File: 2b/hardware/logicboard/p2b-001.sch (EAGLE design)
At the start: 72 parts, among them IC1 74LS06N, IC2 4066N, J1 MKR, J10 1-Wire, J2 GPIO, J3 Vcc, J4** RLY2, J5 SPI, J6 LED, J7 DIN5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

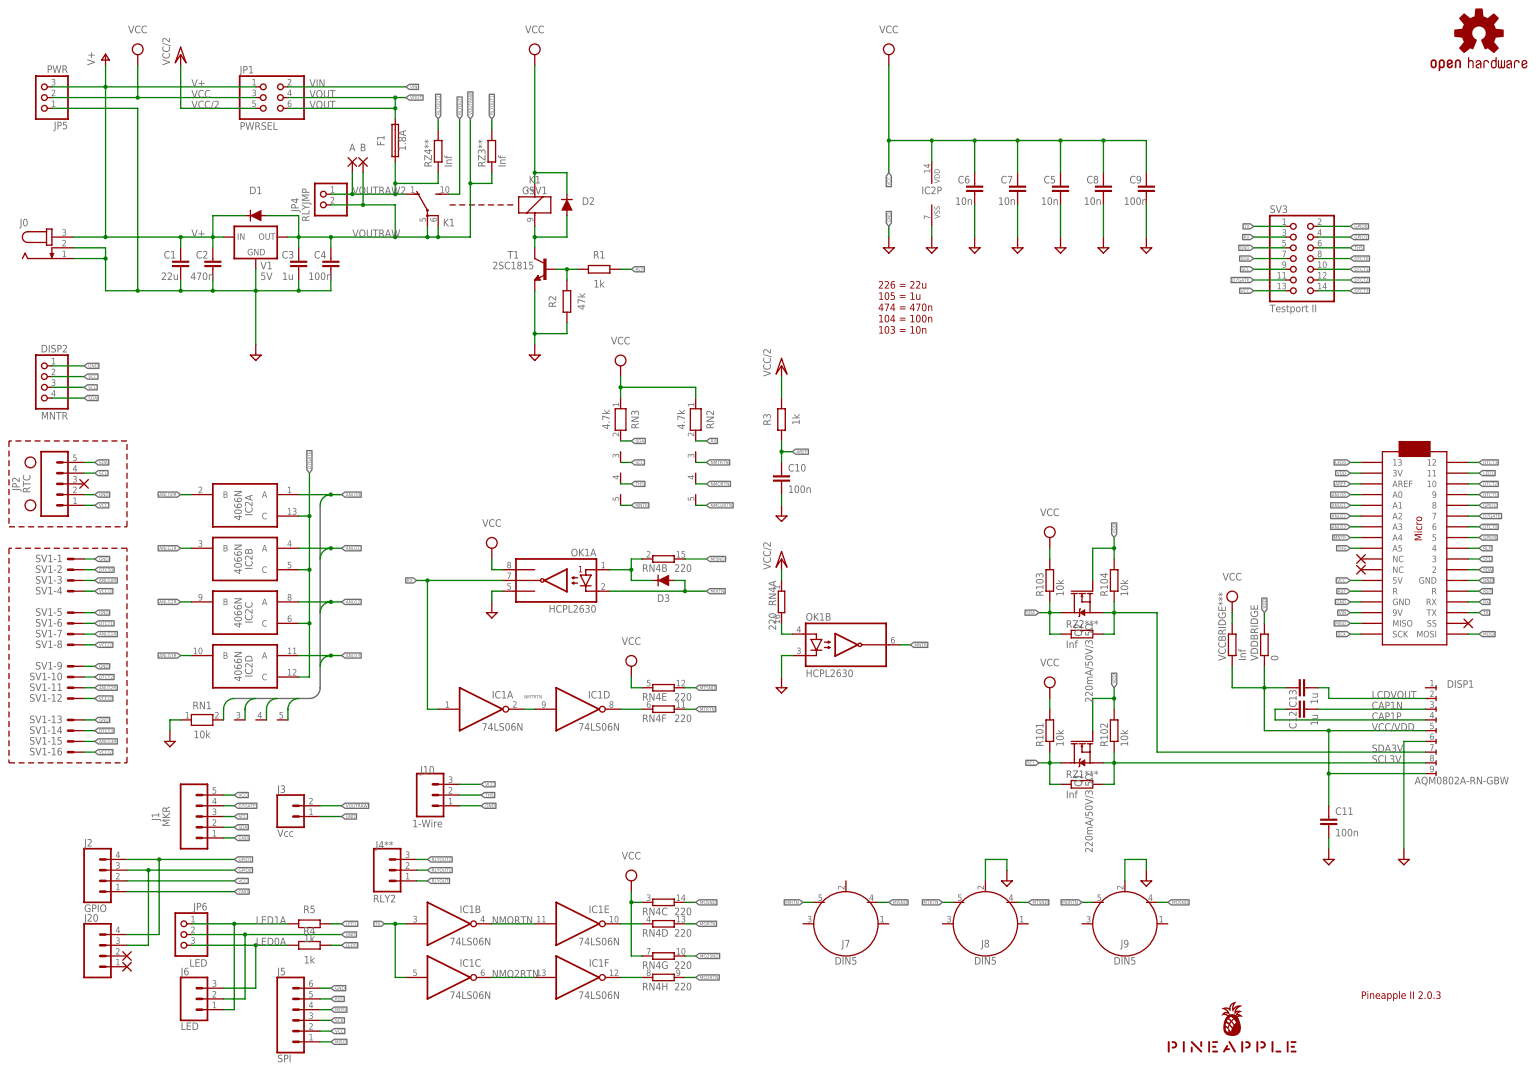
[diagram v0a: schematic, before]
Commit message: Added RST sw to P2b.
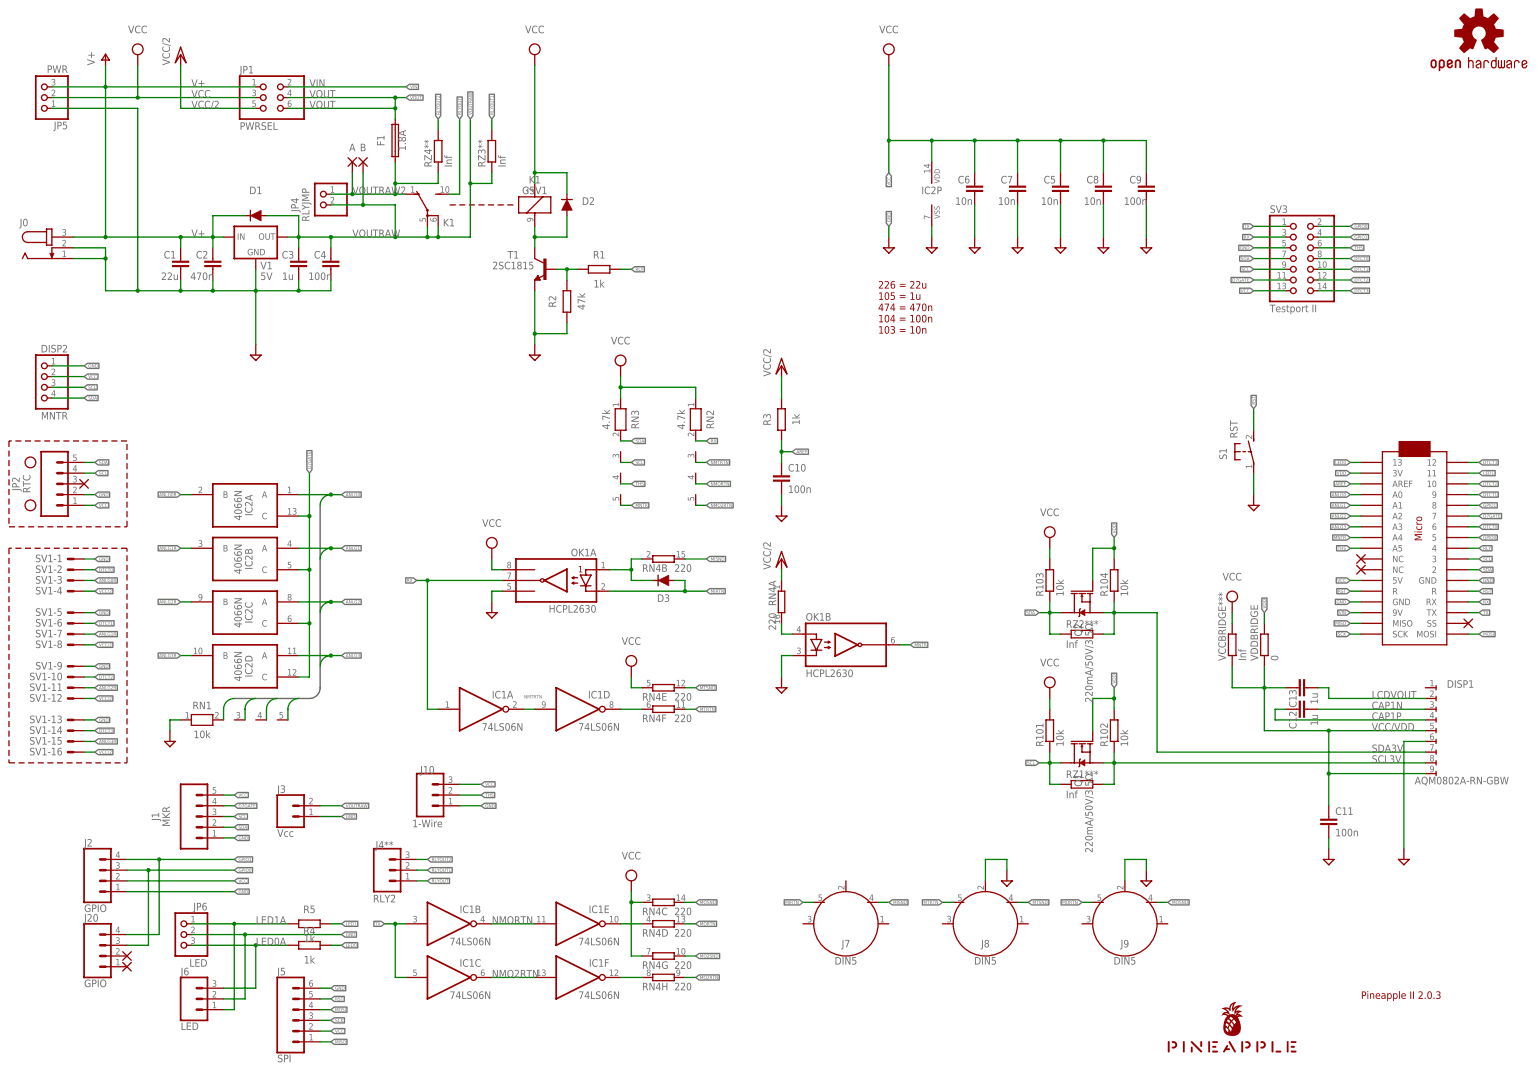
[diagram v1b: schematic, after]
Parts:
- added S1: RST, switch-omron:31-XX
- J20: value (none) -> GPIO
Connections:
- net GND: now also S1.P
- net RST: now also S1.S
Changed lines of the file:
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@@
 <setting verticaltext="up"/>
 </settings>
-<grid distance="0.1" unitdist="inch" unit="inch" style="dots" multiple="1" display="yes" altdistance="0.01" altunitdist="inch" altunit="inch"/>
+<grid distance="0.1" unitdist="inch" unit="inch" style="lines" multiple="1" display="no" altdistance="0.01" altunitdist="inch" altunit="inch"/>
 <layers>
 <layer number="1" name="Top" color="4" fill="1" visible="no" active="no"/>
@@
 <part name="J5" library="SparkFun-Connectors" library_urn="urn:adsk.eagle:library:513" deviceset="CONN_06" device="1.27MM" package3d_urn="urn:adsk.eagle:package:38131/1" value="SPI"/>
 <part name="J10" library="SparkFun-Connectors" library_urn="urn:adsk.eagle:library:513" deviceset="CONN_03" device="JST-PTH-VERT" package3d_urn="urn:adsk.eagle:package:38080/1" value="1-Wire"/>
-<part name="J20" library="SparkFun-Connectors" library_urn="urn:adsk.eagle:library:513" deviceset="CONN_04" device="1.27MM" package3d_urn="urn:adsk.eagle:package:38086/1"/>
+<part name="J20" library="SparkFun-Connectors" library_urn="urn:adsk.eagle:library:513" deviceset="CONN_04" device="1.27MM" package3d_urn="urn:adsk.eagle:package:38086/1" value="GPIO"/>
 <part name="X1" library="wirepad" library_urn="urn:adsk.eagle:library:412" deviceset="PAD-N" device=""/>
 <part name="X2" library="wirepad" library_urn="urn:adsk.eagle:library:412" deviceset="PAD-N" device=""/>
+<part name="S1" library="switch-omron" library_urn="urn:adsk.eagle:library:377" deviceset="31-XX" device="" package3d_urn="urn:adsk.eagle:package:27487/1" value="RST"/>
+<part name="SUPPLY18" library="supply2" deviceset="GND" device=""/>
 </parts>
 <sheets>
@@
 <instance part="X1" gate="G$1" x="50.8" y="30.48" smashed="yes"/>
 <instance part="X2" gate="G$1" x="50.8" y="27.94" smashed="yes"/>
+<instance part="S1" gate="1" x="317.5" y="149.86" smashed="yes">
+<attribute name="NAME" x="311.15" y="147.955" size="1.778" layer="95" rot="R90"/>
+<attribute name="VALUE" x="313.69" y="153.035" size="1.778" layer="96" rot="R90"/>
+</instance>
+<instance part="SUPPLY18" gate="GND" x="317.5" y="137.16" smashed="yes"/>
 </instances>
 <busses>
@@
 <label x="134.62" y="66.04" size="0.8128" layer="95" xref="yes"/>
 </segment>
+<segment>
+<pinref part="S1" gate="1" pin="P"/>
+<wire x1="317.5" y1="144.78" x2="317.5" y2="139.7" width="0.1524" layer="91"/>
+<pinref part="SUPPLY18" gate="GND" pin="GND"/>
+</segment>
 </net>
 <net name="VCC" class="2">
@@
 <pinref part="J5" gate="G$1" pin="5"/>
 </segment>
+<segment>
+<pinref part="S1" gate="1" pin="S"/>
+<wire x1="317.5" y1="154.94" x2="317.5" y2="160.02" width="0.1524" layer="91"/>
+<label x="317.5" y="160.02" size="0.8128" layer="95" rot="R90" xref="yes"/>
+</segment>
 </net>

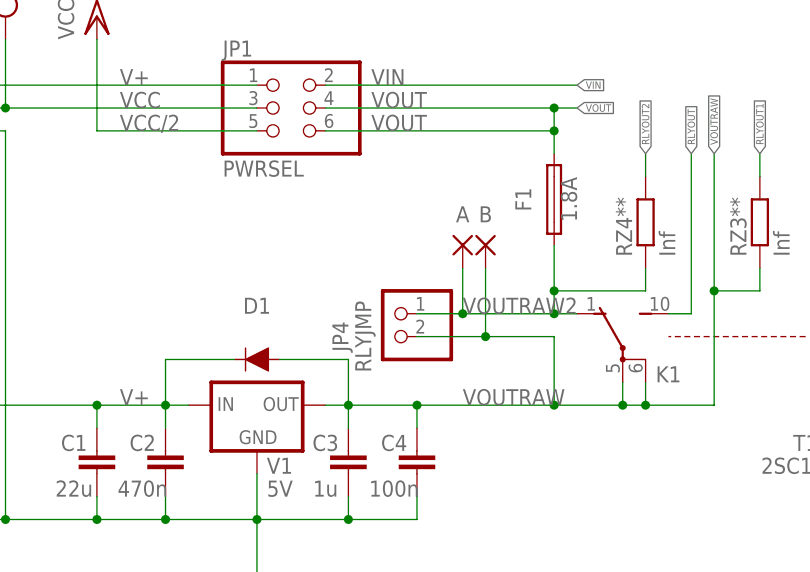
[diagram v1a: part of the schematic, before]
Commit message: Changed pads to Inf-ohm chip resistor.
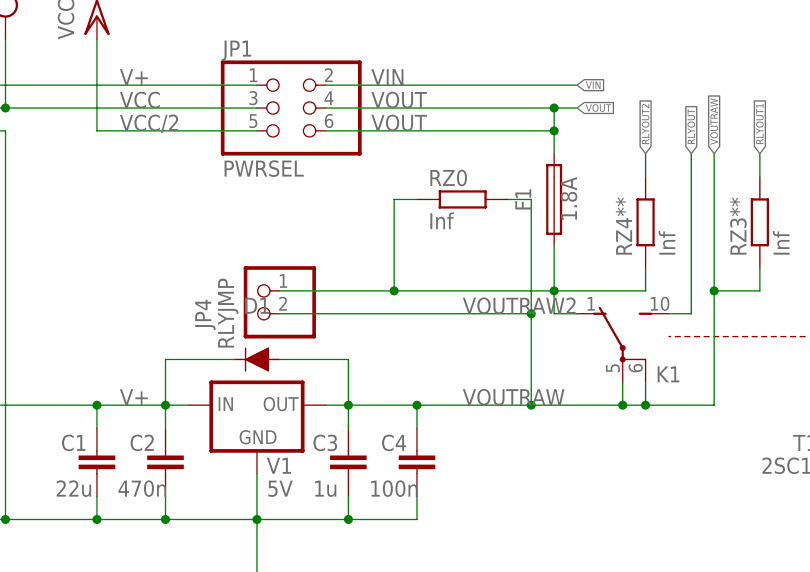
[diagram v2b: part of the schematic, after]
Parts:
- removed A, B: (no value), wirepad:SMD2
- added RZ0: Inf, rcl:R-EU_M2012
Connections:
- net VOUTRAW: now also RZ0.2; no longer B.P
- net VOUTRAW2: now also RZ0.1; no longer A.P
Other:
- moved on the sheet: JP4
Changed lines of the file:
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@@
 <part name="P+3" library="supply1" library_urn="urn:adsk.eagle:library:371" deviceset="V+" device=""/>
 <part name="J6" library="SparkFun-Connectors" library_urn="urn:adsk.eagle:library:513" deviceset="CONN_03" device="JST-PTH-VERT" package3d_urn="urn:adsk.eagle:package:38080/1" value="LED"/>
-<part name="A" library="wirepad" library_urn="urn:adsk.eagle:library:412" deviceset="SMD2" device="" package3d_urn="urn:adsk.eagle:package:30839/1"/>
-<part name="B" library="wirepad" library_urn="urn:adsk.eagle:library:412" deviceset="SMD2" device="" package3d_urn="urn:adsk.eagle:package:30839/1"/>
 <part name="SV3" library="pinhead" library_urn="urn:adsk.eagle:library:325" deviceset="PINHD-2X7" device="" package3d_urn="urn:adsk.eagle:package:22478/2" value="Testport II"/>
 <part name="SUPPLY8" library="supply2" library_urn="urn:adsk.eagle:library:372" deviceset="VCC" device=""/>
@@
 <part name="S1" library="switch-omron" library_urn="urn:adsk.eagle:library:377" deviceset="31-XX" device="" package3d_urn="urn:adsk.eagle:package:27487/1" value="RST"/>
 <part name="SUPPLY18" library="supply2" deviceset="GND" device=""/>
+<part name="RZ0" library="rcl" library_urn="urn:adsk.eagle:library:334" deviceset="R-EU_" device="M2012" package3d_urn="urn:adsk.eagle:package:23561/2" value="Inf"/>
 </parts>
 <sheets>
@@
 </instance>
 <instance part="SUPPLY11" gate="GND" x="241.3" y="198.12" smashed="yes"/>
-<instance part="JP4" gate="G$1" x="96.52" y="208.28" smashed="yes" rot="MR0">
-<attribute name="NAME" x="91.44" y="208.28" size="1.778" layer="95" rot="R90" align="bottom-center"/>
-<attribute name="VALUE" x="93.98" y="208.28" size="1.778" layer="96" rot="R90" align="bottom-center"/>
+<instance part="JP4" gate="G$1" x="81.28" y="210.82" smashed="yes" rot="MR0">
+<attribute name="NAME" x="76.2" y="210.82" size="1.778" layer="95" rot="R90" align="bottom-center"/>
+<attribute name="VALUE" x="78.74" y="210.82" size="1.778" layer="96" rot="R90" align="bottom-center"/>
 </instance>
 <instance part="SUPPLY29" gate="GND" x="137.16" y="111.76" smashed="yes"/>
@@
 <attribute name="NAME" x="63.5" y="25.908" size="1.778" layer="95" font="vector"/>
 </instance>
-<instance part="A" gate="1" x="104.14" y="218.44" smashed="yes" rot="R270">
-<attribute name="NAME" x="104.14" y="220.98" size="1.778" layer="95" align="bottom-center"/>
-<attribute name="VALUE" x="100.838" y="219.583" size="1.778" layer="96" rot="R270"/>
-</instance>
-<instance part="B" gate="1" x="106.68" y="218.44" smashed="yes" rot="R270">
-<attribute name="NAME" x="106.68" y="220.98" size="1.778" layer="95" align="bottom-center"/>
-<attribute name="VALUE" x="103.378" y="219.583" size="1.778" layer="96" rot="R270"/>
-</instance>
 <instance part="SV3" gate="A" x="327.66" y="195.58" smashed="yes">
 <attribute name="NAME" x="321.31" y="206.375" size="1.778" layer="95"/>
@@
 </instance>
 <instance part="SUPPLY18" gate="GND" x="317.5" y="137.16" smashed="yes"/>
+<instance part="RZ0" gate="G$1" x="104.14" y="223.52" smashed="yes">
+<attribute name="NAME" x="100.33" y="225.0186" size="1.778" layer="95"/>
+<attribute name="VALUE" x="100.33" y="220.218" size="1.778" layer="96"/>
+</instance>
 </instances>
 <busses>
@@
 <wire x1="114.3" y1="210.82" x2="116.84" y2="210.82" width="0.1524" layer="91"/>
 <pinref part="JP4" gate="G$1" pin="1"/>
-<wire x1="114.3" y1="210.82" x2="104.14" y2="210.82" width="0.1524" layer="91"/>
-<junction x="114.3" y="210.82"/>
-<pinref part="A" gate="1" pin="P"/>
-<wire x1="104.14" y1="210.82" x2="99.06" y2="210.82" width="0.1524" layer="91"/>
-<wire x1="104.14" y1="215.9" x2="104.14" y2="210.82" width="0.1524" layer="91"/>
-<junction x="104.14" y="210.82"/>
+<wire x1="96.52" y1="213.36" x2="83.82" y2="213.36" width="0.1524" layer="91"/>
+<junction x="96.52" y="213.36"/>
 <label x="104.14" y="210.82" size="1.778" layer="95"/>
 <pinref part="RZ4**" gate="G$1" pin="1"/>
@@
 <wire x1="124.46" y1="213.36" x2="114.3" y2="213.36" width="0.1524" layer="91"/>
 <junction x="114.3" y="213.36"/>
+<pinref part="RZ0" gate="G$1" pin="1"/>
+<wire x1="99.06" y1="223.52" x2="96.52" y2="223.52" width="0.1524" layer="91"/>
+<wire x1="96.52" y1="223.52" x2="96.52" y2="213.36" width="0.1524" layer="91"/>
+<wire x1="96.52" y1="213.36" x2="114.3" y2="213.36" width="0.1524" layer="91"/>
 </segment>
 </net>
@@
 <pinref part="V1" gate="A" pin="OUT"/>
 <wire x1="124.46" y1="200.66" x2="121.92" y2="200.66" width="0.1524" layer="91"/>
-<wire x1="121.92" y1="200.66" x2="114.3" y2="200.66" width="0.1524" layer="91"/>
-<wire x1="114.3" y1="200.66" x2="99.06" y2="200.66" width="0.1524" layer="91"/>
+<wire x1="121.92" y1="200.66" x2="111.76" y2="200.66" width="0.1524" layer="91"/>
+<wire x1="111.76" y1="200.66" x2="99.06" y2="200.66" width="0.1524" layer="91"/>
 <wire x1="99.06" y1="200.66" x2="91.44" y2="200.66" width="0.1524" layer="91"/>
 <wire x1="91.44" y1="200.66" x2="88.9" y2="200.66" width="0.1524" layer="91"/>
@@
 <junction x="121.92" y="200.66"/>
 <pinref part="JP4" gate="G$1" pin="2"/>
-<wire x1="99.06" y1="208.28" x2="106.68" y2="208.28" width="0.1524" layer="91"/>
-<wire x1="106.68" y1="208.28" x2="114.3" y2="208.28" width="0.1524" layer="91"/>
-<wire x1="114.3" y1="208.28" x2="114.3" y2="200.66" width="0.1524" layer="91"/>
-<junction x="114.3" y="200.66"/>
+<wire x1="83.82" y1="210.82" x2="111.76" y2="210.82" width="0.1524" layer="91"/>
+<wire x1="111.76" y1="210.82" x2="111.76" y2="200.66" width="0.1524" layer="91"/>
+<junction x="111.76" y="200.66"/>
 <wire x1="124.46" y1="200.66" x2="132.08" y2="200.66" width="0.1524" layer="91"/>
 <junction x="124.46" y="200.66"/>
 <wire x1="132.08" y1="200.66" x2="132.08" y2="213.36" width="0.1524" layer="91"/>
 <label x="132.08" y="228.6" size="0.8128" layer="95" rot="R90" xref="yes"/>
-<pinref part="B" gate="1" pin="P"/>
 <wire x1="132.08" y1="213.36" x2="132.08" y2="228.6" width="0.1524" layer="91"/>
-<wire x1="106.68" y1="215.9" x2="106.68" y2="208.28" width="0.1524" layer="91"/>
-<junction x="106.68" y="208.28"/>
+<junction x="111.76" y="210.82"/>
 <pinref part="RZ3**" gate="G$1" pin="1"/>
 <wire x1="137.16" y1="213.36" x2="137.16" y2="215.9" width="0.1524" layer="91"/>
@@
 <junction x="132.08" y="213.36"/>
 <label x="104.14" y="200.66" size="1.778" layer="95"/>
-</segment>
-<segment>
+<pinref part="RZ0" gate="G$1" pin="2"/>
+<wire x1="109.22" y1="223.52" x2="111.76" y2="223.52" width="0.1524" layer="91"/>
+<wire x1="111.76" y1="223.52" x2="111.76" y2="210.82" width="0.1524" layer="91"/>
+</segment>
+<segment>

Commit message: Fixed P2b.
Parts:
- added RZ01, RZ02, RZ03, RZ04: Inf, rcl:R-EU_M2012
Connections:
- net ANLG0: now also RZ01.2
- net ANLG0R: now also RZ01.1
- net ANLG1: now also RZ02.2
- net ANLG1R: now also RZ02.1
- net ANLG2: now also RZ03.2
- net ANLG2R: now also RZ03.1
- net ANLG3: now also RZ04.2
- net ANLG3R: now also RZ04.1
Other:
- moved on the sheet: IC2A, IC2B, IC2C, IC2D

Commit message: Fixed caps.
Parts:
- C1: value 22u -> 10u; device rcl:C-EU025-050X050 -> rcl:C-EU025-030X050
- C2: value 470n -> 100n; device rcl:C-EU050-024X044 -> rcl:C-EU025-024X044
- C3: value 1u -> 47u; device rcl:C-EU050-024X044 -> rcl:C-EU025-050X050
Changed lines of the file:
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@@
 <part name="SUPPLY12" library="supply2" deviceset="GND" device=""/>
 <part name="X4" library="wirepad" library_urn="urn:adsk.eagle:library:412" deviceset="PAD-N" device=""/>
-<part name="C2" library="rcl" library_urn="urn:adsk.eagle:library:334" deviceset="C-EU" device="050-024X044" package3d_urn="urn:adsk.eagle:package:23643/1" value="470n"/>
+<part name="C2" library="rcl" library_urn="urn:adsk.eagle:library:334" deviceset="C-EU" device="025-024X044" package3d_urn="urn:adsk.eagle:package:23630/1" value="100n"/>
 <part name="C4" library="rcl" library_urn="urn:adsk.eagle:library:334" deviceset="C-EU" device="025-024X044" package3d_urn="urn:adsk.eagle:package:23630/1" value="100n"/>
 <part name="C6" library="resistor" library_urn="urn:adsk.eagle:library:348" deviceset="C-EU" device="025-024X044" package3d_urn="urn:adsk.eagle:package:23630/1" value="10n"/>
 <part name="C7" library="resistor" library_urn="urn:adsk.eagle:library:348" deviceset="C-EU" device="025-024X044" package3d_urn="urn:adsk.eagle:package:23630/1" value="10n"/>
-<part name="C1" library="rcl" library_urn="urn:adsk.eagle:library:334" deviceset="C-EU" device="025-050X050" package3d_urn="urn:adsk.eagle:package:23633/1" value="22u"/>
-<part name="C3" library="rcl" library_urn="urn:adsk.eagle:library:334" deviceset="C-EU" device="050-024X044" package3d_urn="urn:adsk.eagle:package:23643/1" value="1u"/>
+<part name="C1" library="rcl" library_urn="urn:adsk.eagle:library:334" deviceset="C-EU" device="025-030X050" package3d_urn="urn:adsk.eagle:package:23631/1" value="10u"/>
+<part name="C3" library="rcl" library_urn="urn:adsk.eagle:library:334" deviceset="C-EU" device="025-050X050" package3d_urn="urn:adsk.eagle:package:23633/1" value="47u"/>
 <part name="SUPPLY23" library="supply2" deviceset="GND" device=""/>
 <part name="F1" library="fuse" library_urn="urn:adsk.eagle:library:233" deviceset="TE5" device="" package3d_urn="urn:adsk.eagle:package:14069/1" value="1.8A"/>
